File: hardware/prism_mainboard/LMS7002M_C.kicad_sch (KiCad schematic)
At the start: 1 part, among them U2 LMS7002M

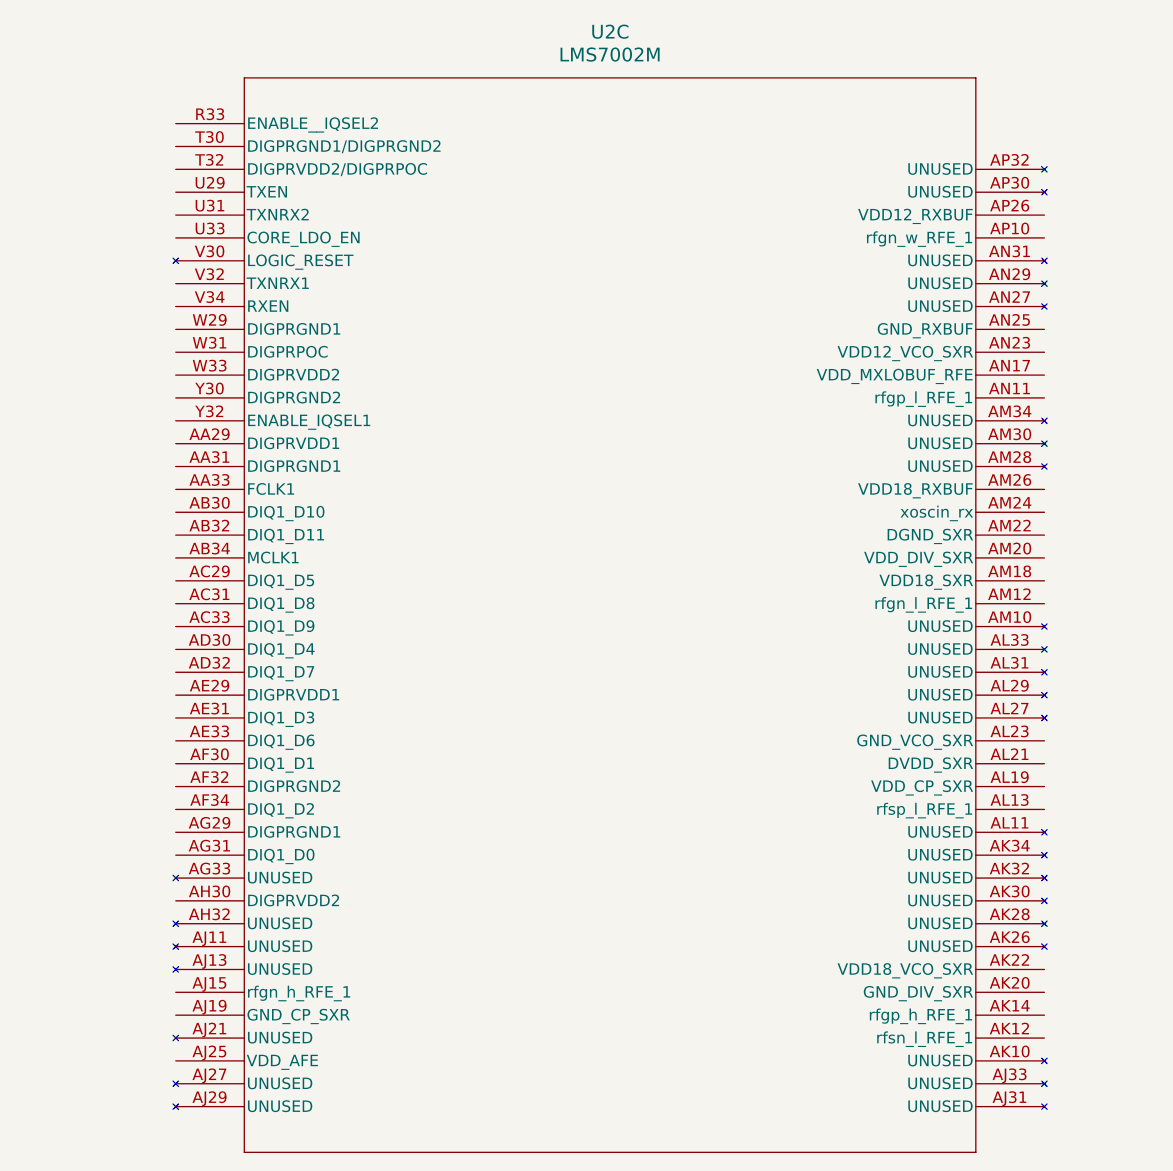
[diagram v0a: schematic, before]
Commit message: Mainboard Updates
Started a lot of the basic schematic nets like GND and Power nets. Major Change: Decided on using the XC7Z015-1CLG485I instead of the 7010 or 7020 due to the ability to use HDMI interfaces with an adapter and more LUTs. Updated schematic symbols and footprints accordingly. Added Memory, Encoder, MicroSD schematics. Added LimeSDR footprints as well. Will Try to add Power to the entire board next.
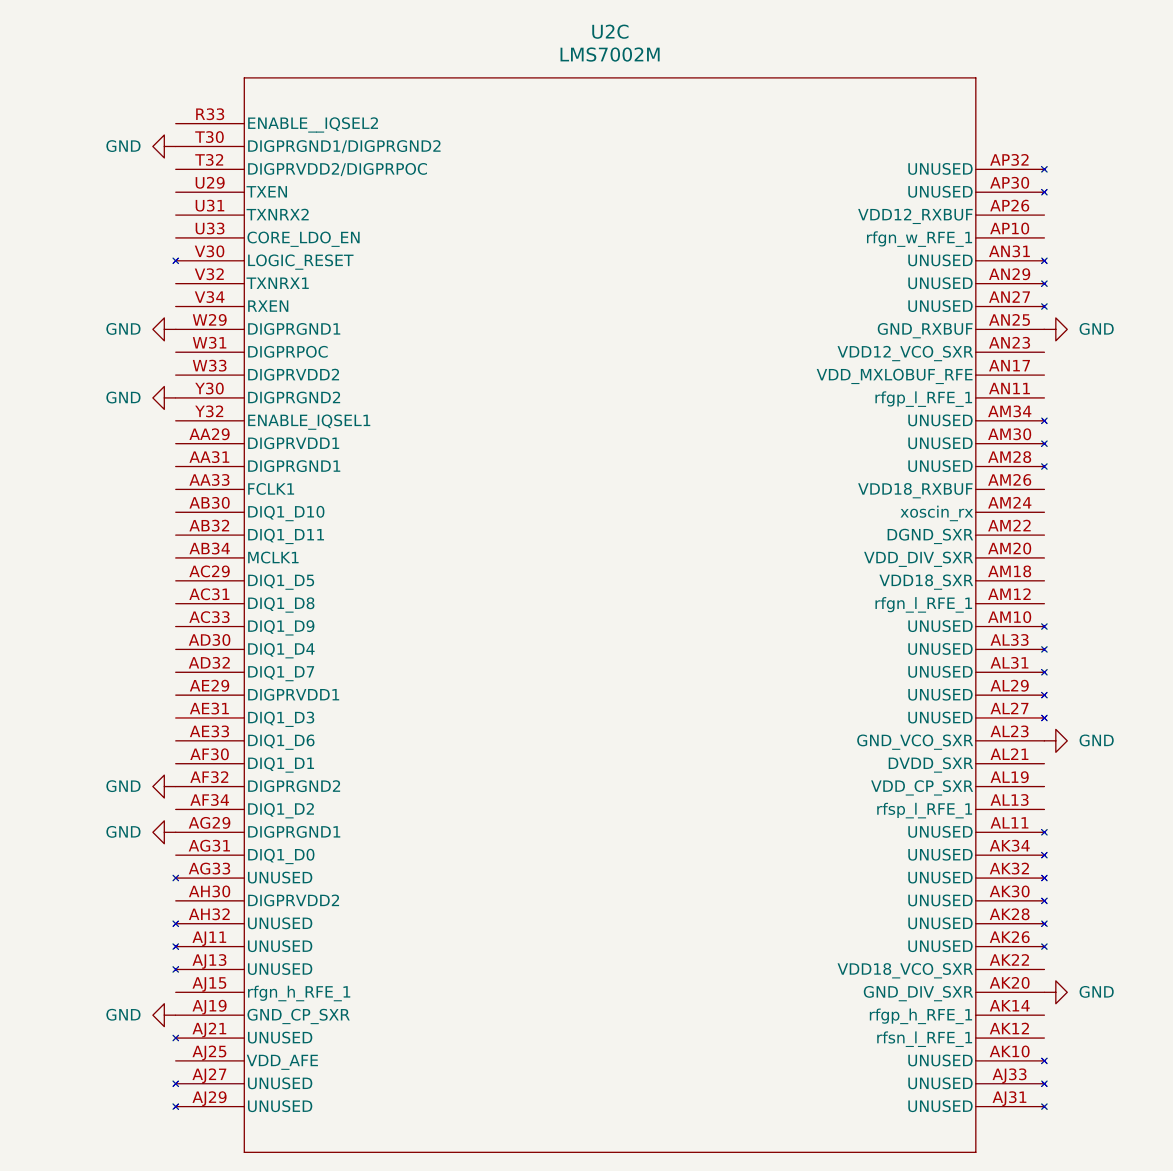
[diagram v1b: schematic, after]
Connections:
- net GND: now reaches U2.AF32 (DIGPRGND2)
- net GND: now also U2.AG29 (DIGPRGND1), U2.AJ19 (GND_CP_SXR), U2.AK20 (GND_DIV_SXR), U2.AL23 (GND_VCO_SXR), U2.AN25 (GND_RXBUF), U2.T30 (DIGPRGND1/DIGPRGND2), U2.W29 (DIGPRGND1), U2.Y30 (DIGPRGND2)

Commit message: Schematic Updates
Updated schematics. Most of the power and decoupling is set for most if not all devices. Need to interconnect devices. Still reading datasheets
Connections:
- net VDD_1V8_DIG: now reaches U2.AH30 (DIGPRVDD2)
- net VDD_1V8_DIG: now also U2.T32 (DIGPRVDD2/DIGPRPOC)
- net VDD_1V8: now reaches U2.AK22 (VDD18_VCO_SXR)
- net VDD_1V8: now also U2.AM18 (VDD18_SXR), U2.AM26 (VDD18_RXBUF)
- net NC: now reaches U2.U33 (CORE_LDO_EN)
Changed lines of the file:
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@@
 	(generator_version "10.0")
 	(paper "A4")
+	(global_label "VDD_1V8_DIG"
+		(shape input)
+		(at 97.79 123.19 180)
+		(fields_autoplaced yes)
+		(effects
+			(font
+				(size 1.27 1.27)
+			)
+			(justify right)
+		)
+		(property "Intersheetrefs" "${INTERSHEET_REFS}"
+			(at 82.5886 123.19 0)
+			(hide yes)
+			(show_name no)
+			(do_not_autoplace no)
+			(effects
+				(font
+					(size 1.27 1.27)
+				)
+				(justify right)
+			)
+		)
+	)
+	(global_label "NC"
+		(shape input)
+		(at 97.79 49.53 180)
+		(fields_autoplaced yes)
+		(effects
+			(font
+				(size 1.27 1.27)
+			)
+			(justify right)
+		)
+		(property "Intersheetrefs" "${INTERSHEET_REFS}"
+			(at 92.2043 49.53 0)
+			(hide yes)
+			(show_name no)
+			(do_not_autoplace no)
+			(effects
+				(font
+					(size 1.27 1.27)
+				)
+				(justify right)
+			)
+		)
+	)
+	(global_label "VDD_1V8"
+		(shape input)
+		(at 194.31 130.81 0)
+		(fields_autoplaced yes)
+		(effects
+			(font
+				(size 1.27 1.27)
+			)
+			(justify left)
+		)
+		(property "Intersheetrefs" "${INTERSHEET_REFS}"
+			(at 205.399 130.81 0)
+			(hide yes)
+			(show_name no)
+			(do_not_autoplace no)
+			(effects
+				(font
+					(size 1.27 1.27)
+				)
+				(justify left)
+			)
+		)
+	)
+	(global_label "VDD_1V8"
+		(shape input)
+		(at 194.31 77.47 0)
+		(fields_autoplaced yes)
+		(effects
+			(font
+				(size 1.27 1.27)
+			)
+			(justify left)
+		)
+		(property "Intersheetrefs" "${INTERSHEET_REFS}"
+			(at 205.399 77.47 0)
+			(hide yes)
+			(show_name no)
+			(do_not_autoplace no)
+			(effects
+				(font
+					(size 1.27 1.27)
+				)
+				(justify left)
+			)
+		)
+	)
+	(global_label "VDD_1V8"
+		(shape input)
+		(at 194.31 87.63 0)
+		(fields_autoplaced yes)
+		(effects
+			(font
+				(size 1.27 1.27)
+			)
+			(justify left)
+		)
+		(property "Intersheetrefs" "${INTERSHEET_REFS}"
+			(at 205.399 87.63 0)
+			(hide yes)
+			(show_name no)
+			(do_not_autoplace no)
+			(effects
+				(font
+					(size 1.27 1.27)
+				)
+				(justify left)
+			)
+		)
+	)
+	(global_label "VDD_1V8_DIG"
+		(shape input)
+		(at 97.79 41.91 180)
+		(fields_autoplaced yes)
+		(effects
+			(font
+				(size 1.27 1.27)
+			)
+			(justify right)
+		)
+		(property "Intersheetrefs" "${INTERSHEET_REFS}"
+			(at 82.5886 41.91 0)
+			(hide yes)
+			(show_name no)
+			(do_not_autoplace no)
+			(effects
+				(font
+					(size 1.27 1.27)
+				)
+				(justify right)
+			)
+		)
+	)
 	(symbol
 		(lib_id "2026-05-17_20-58-30:LMS7002M")

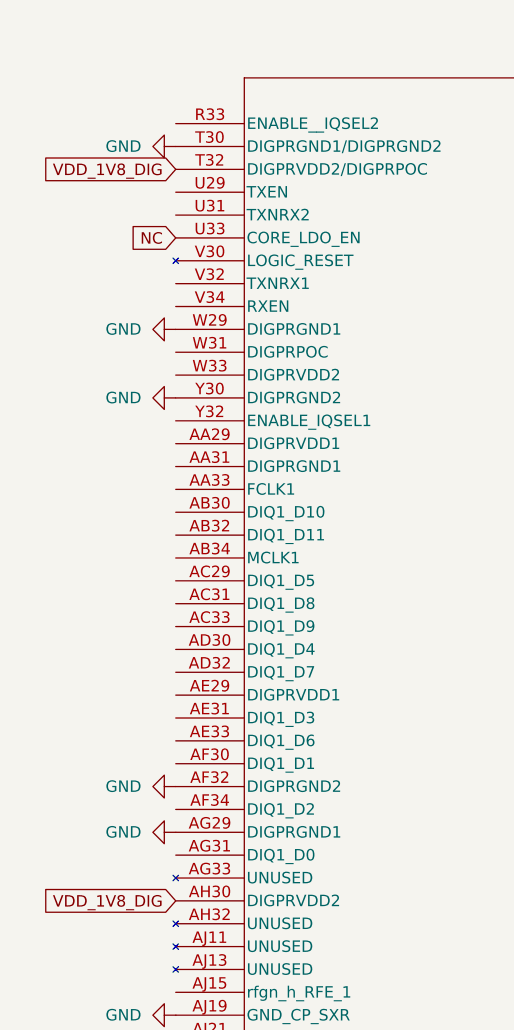
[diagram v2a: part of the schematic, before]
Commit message: Schematic Updates
Added the LMS7002M to XC7Z015 connections, atleast the preliminary data connections.
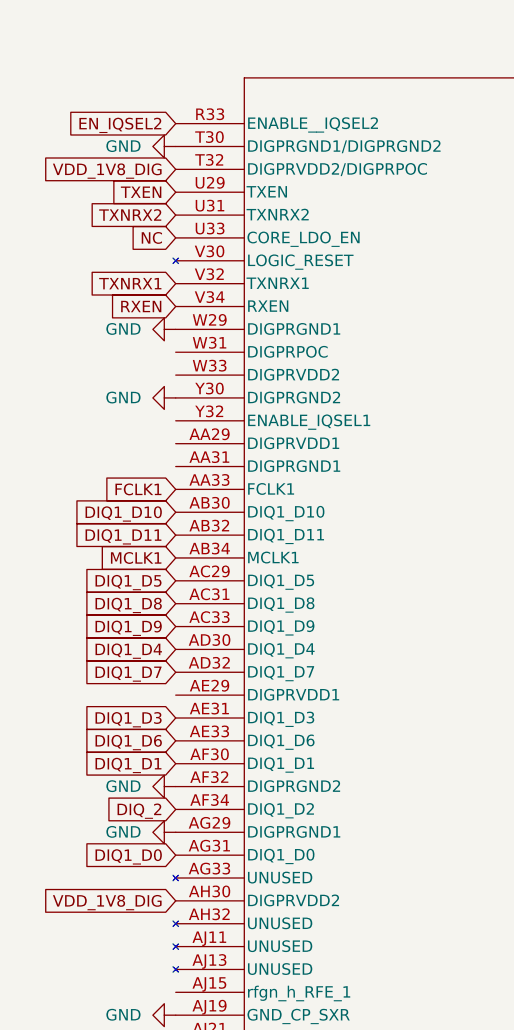
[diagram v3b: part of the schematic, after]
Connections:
- net FCLK1: now reaches U2.AA33 (FCLK1)
- net DIQ1_D10: now reaches U2.AB30 (DIQ1_D10)
- net DIQ1_D11: now reaches U2.AB32 (DIQ1_D11)
- net MCLK1: now reaches U2.AB34 (MCLK1)
- net DIQ1_D5: now reaches U2.AC29 (DIQ1_D5)
- net DIQ1_D8: now reaches U2.AC31 (DIQ1_D8)
- net DIQ1_D9: now reaches U2.AC33 (DIQ1_D9)
- net DIQ1_D4: now reaches U2.AD30 (DIQ1_D4)
- net DIQ1_D7: now reaches U2.AD32 (DIQ1_D7)
- net DIQ1_D3: now reaches U2.AE31 (DIQ1_D3)
- net DIQ1_D6: now reaches U2.AE33 (DIQ1_D6)
- net DIQ1_D1: now reaches U2.AF30 (DIQ1_D1)
- net DIQ_2: now reaches U2.AF34 (DIQ1_D2)
- net DIQ1_D0: now reaches U2.AG31 (DIQ1_D0)
- net EN_IQSEL2: now reaches U2.R33 (ENABLE__IQSEL2)
- net TXEN: now reaches U2.U29 (TXEN)
- net TXNRX2: now reaches U2.U31 (TXNRX2)
- net TXNRX1: now reaches U2.V32 (TXNRX1)
- net RXEN: now reaches U2.V34 (RXEN)

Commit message: Updates
Mostly Schematic updates, nothing too big. Added a few datasheets
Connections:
- net EN_IQSEL1: now reaches U2.Y32 (ENABLE_IQSEL1)
- net DIQ_2 renamed DIQ1_D2
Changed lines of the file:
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@@
+		)
+	)
+	(global_label "EN_IQSEL1"
+		(shape input)
+		(at 97.79 69.85 180)
+		(fields_autoplaced yes)
+		(effects
+			(font
+				(size 1.27 1.27)
+			)
+			(justify right)
+		)
+		(property "Intersheetrefs" "${INTERSHEET_REFS}"
+			(at 84.8263 69.85 0)
+			(hide yes)
+			(show_name no)
+			(do_not_autoplace no)
+			(effects
+				(font
+					(size 1.27 1.27)
+				)
+				(justify right)
+			)
 		)
 	)
@@
 		)
 	)
-	(global_label "DIQ_2"
+	(global_label "DIQ1_D2"
 		(shape input)
 		(at 97.79 113.03 180)
@@
 		)
 		(property "Intersheetrefs" "${INTERSHEET_REFS}"
-			(at 89.4224 113.03 0)
-			(hide yes)
-			(show_name no)
+			(at 86.9429 113.03 0)
+			(hide yes)
+			(show_name no)
